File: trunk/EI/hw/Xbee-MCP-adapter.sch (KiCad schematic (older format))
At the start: 10 parts

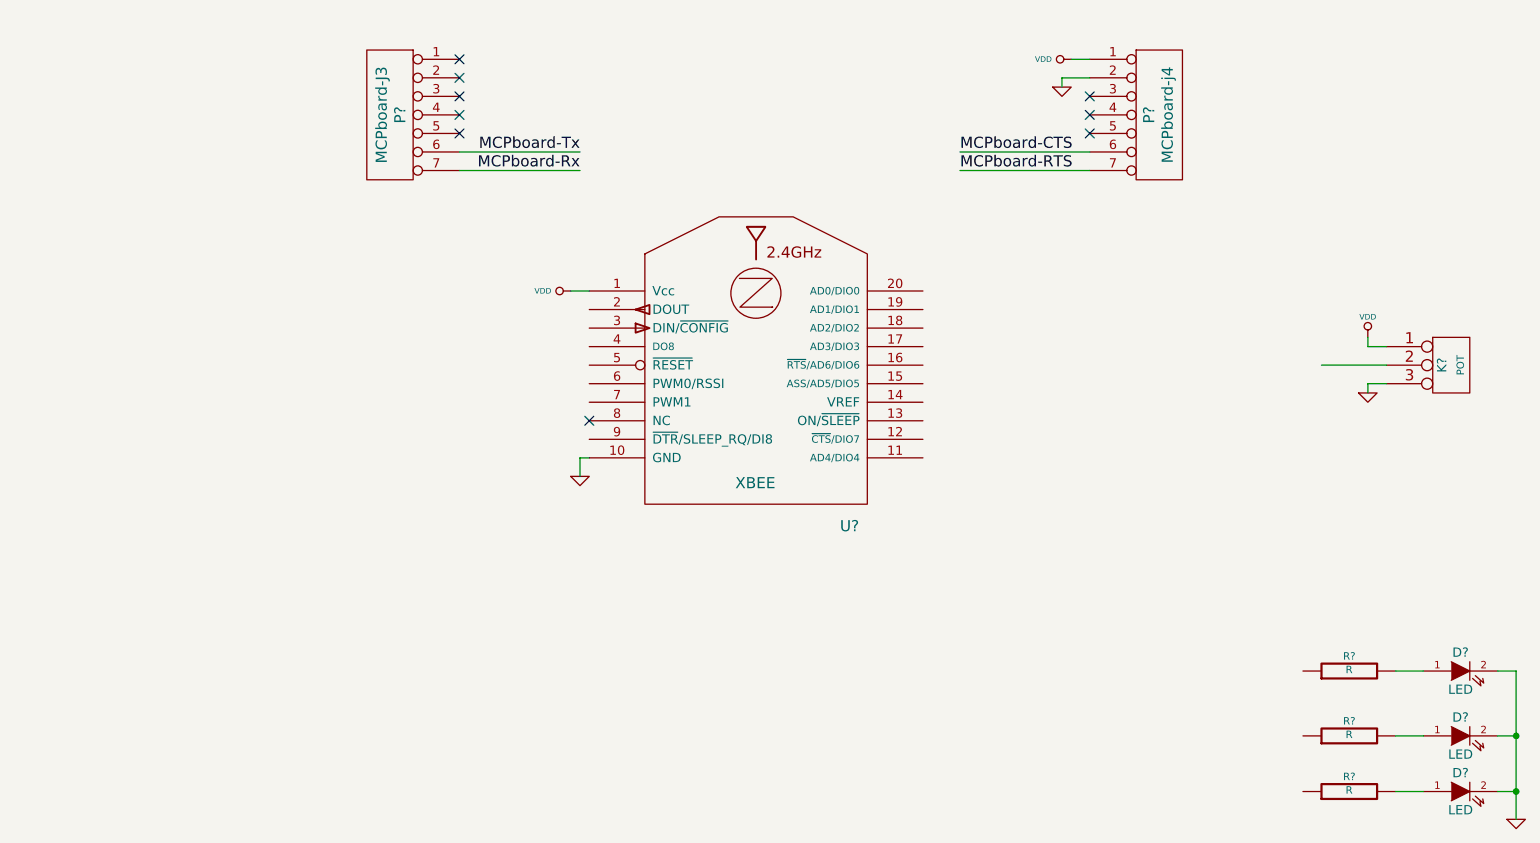
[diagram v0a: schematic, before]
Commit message: La primera version de la placa Xbee-MCP-adapter
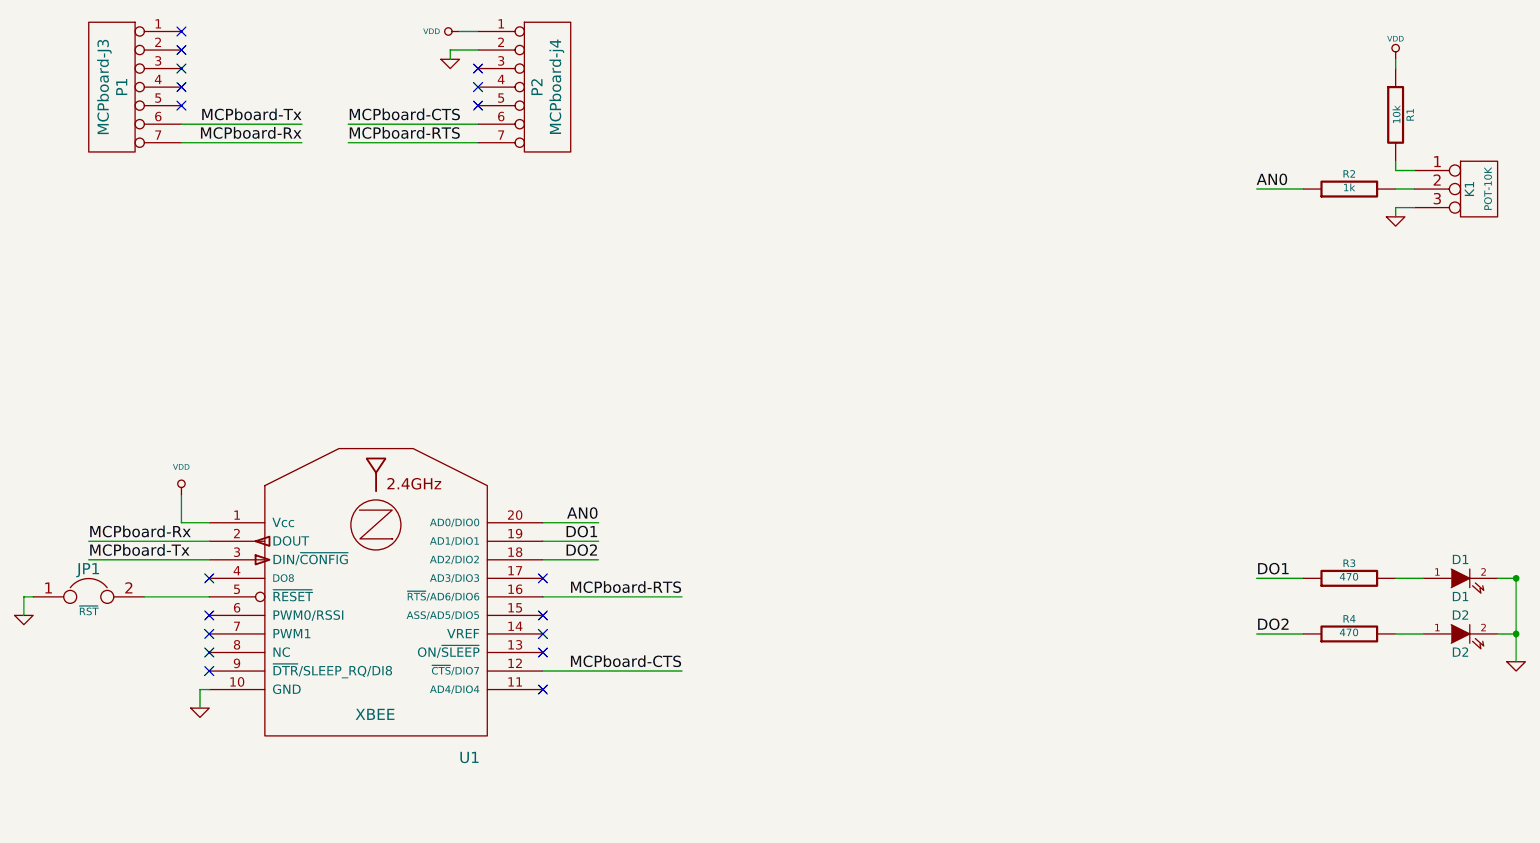
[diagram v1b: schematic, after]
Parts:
- removed D?: LED, ~, symbol LED
- removed R?: R, ~, symbol R
- added JP1: ~RST, ~, symbol JUMPER
- added R1: 10k, ~, symbol R
- added R2: 1k, ~, symbol R
- D1: renamed from D?; value LED -> D1
- D2: renamed from D?; value LED -> D2
- K1: renamed from K?; value POT -> POT-10K
- R3, R4: renamed from R?; value R -> 470
- gave numbers to parts that had none: 3
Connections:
- net labels added: AN0, DO1, DO2
- wire segments 22 -> 35
- no-connect marks 9 -> 18
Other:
- moved on the sheet: D1, D2, K1, P1, P2, R3, R4, U1
